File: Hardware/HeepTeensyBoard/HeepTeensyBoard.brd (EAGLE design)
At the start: 61 x 54 mm, 31 parts, among them J1 MAGJACK, J4 POWER_JACKPTH, Q1 25MHz, U1 ENC28J60-SO

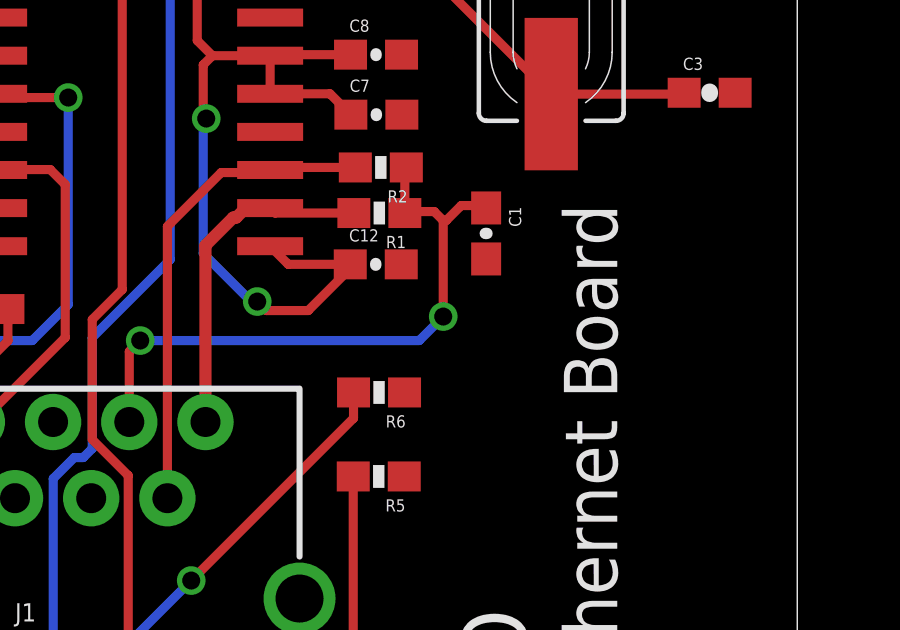
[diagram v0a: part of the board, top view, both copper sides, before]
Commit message: #156 Added a ferrite bead to layout and schematic of pure teensy board
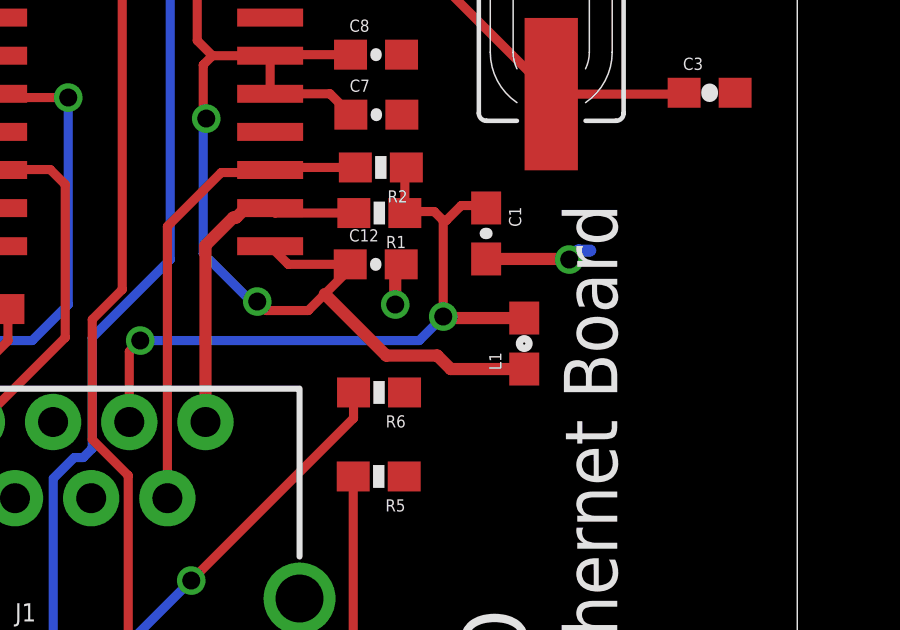
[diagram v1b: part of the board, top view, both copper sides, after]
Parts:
- added L1: (no value), SparkFun-Passives:0603
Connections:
- net 3.3V: now also L1.1
- net N$7: now also L1.2
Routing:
- net 3.3V: track 141.3 -> 148.9 mm
- net GND: track 8.61 -> 13.8 mm, vias 2 -> 4
- net N$7: track 21.1 -> 23.9 mm
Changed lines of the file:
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@@
 <setting verticaltext="up"/>
 </settings>
-<grid distance="1" unitdist="mm" unit="mm" style="lines" multiple="1" display="no" altdistance="0.025" altunitdist="inch" altunit="inch"/>
+<grid distance="0.1" unitdist="mm" unit="mm" style="lines" multiple="1" display="no" altdistance="0.025" altunitdist="inch" altunit="inch"/>
 <layers>
 <layer number="1" name="Top" color="4" fill="1" visible="yes" active="yes"/>
@@
 </element>
 <element name="J5" library="SparkFun-Connectors" package="1X02" value="" x="22" y="46" rot="R90"/>
+<element name="L1" library="SparkFun-Passives" package="0603" value="" x="51.9" y="22.6" rot="R90"/>
 </elements>
 <signals>
@@
 <wire x1="49.8" y1="27.2" x2="50.55" y2="27.2" width="0.3048" layer="1"/>
 <wire x1="50.55" y1="27.2" x2="50.63" y2="27.12" width="0.3048" layer="1"/>
+<contactref element="L1" pad="2"/>
+<wire x1="51.9" y1="23.45" x2="49.2" y2="23.45" width="0.4064" layer="1"/>
+<wire x1="49.2" y1="23.45" x2="49.2" y2="23.5" width="0.4064" layer="1"/>
 </signal>
 <signal name="GND">
@@
 <vertex x="-15" y="-4"/>
 </polygon>
+<wire x1="50.63" y1="25.42" x2="53.38" y2="25.42" width="0.4064" layer="1"/>
+<wire x1="53.38" y1="25.42" x2="53.4" y2="25.4" width="0.4064" layer="1"/>
+<via x="53.4" y="25.4" extent="1-16" drill="0.6" shape="square"/>
+<wire x1="53.4" y1="25.4" x2="53.7" y2="25.7" width="0.4064" layer="16"/>
+<wire x1="53.7" y1="25.7" x2="54.1" y2="25.7" width="0.4064" layer="16"/>
+<wire x1="47.8" y1="25.24" x2="47.6" y2="25.04" width="0.4064" layer="1"/>
+<wire x1="47.6" y1="25.04" x2="47.6" y2="23.9" width="0.4064" layer="1"/>
+<via x="47.6" y="23.9" extent="1-16" drill="0.6" shape="square"/>
+<wire x1="47.6" y1="23.9" x2="47.6" y2="23.7" width="0.4064" layer="16"/>
 <wire x1="43.43" y1="29.655" x2="43.43" y2="33.465" width="0" layer="19" extent="1-1"/>
 </signal>
@@
 <wire x1="43.385" y1="38.5" x2="43.43" y2="38.545" width="0.3048" layer="1"/>
 <wire x1="46.1" y1="25.24" x2="46.1" y2="25.1" width="0.3048" layer="1"/>
-<wire x1="46.1" y1="25.1" x2="44.7" y2="23.7" width="0.3048" layer="1"/>
+<wire x1="46.1" y1="25.1" x2="45.25" y2="24.25" width="0.3048" layer="1"/>
+<wire x1="45.25" y1="24.25" x2="44.7" y2="23.7" width="0.3048" layer="1"/>
 <wire x1="44.7" y1="23.7" x2="43.3" y2="23.7" width="0.3048" layer="1"/>
 <wire x1="43.3" y1="23.7" x2="43" y2="24" width="0.3048" layer="1"/>
@@
 <wire x1="43.5" y1="45.3" x2="26" y2="45.3" width="0.3048" layer="1"/>
 <wire x1="26" y1="45.3" x2="22.55" y2="41.85" width="0.3048" layer="1"/>
+<contactref element="L1" pad="1"/>
+<wire x1="51.9" y1="21.75" x2="49.45" y2="21.75" width="0.4064" layer="1"/>
+<wire x1="49.45" y1="21.75" x2="49" y2="22.2" width="0.4064" layer="1"/>
+<wire x1="49" y1="22.2" x2="47.3" y2="22.2" width="0.4064" layer="1"/>
+<wire x1="47.3" y1="22.2" x2="45.25" y2="24.25" width="0.4064" layer="1"/>
 </signal>
 <signal name="N$15">
